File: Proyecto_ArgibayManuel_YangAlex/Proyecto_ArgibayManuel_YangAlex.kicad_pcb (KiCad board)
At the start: 2 copper layers, 56 parts, among them IC1 LM1117, J1 Con_1x3, J2 Con_1x2, J3 Con_1x3, J4 Conn_01x03_Pin, J5 Conn_01x06, J6 Con_ICSP, K1 RT314012, K2 RT314012, Q1 2N2222, Q2 2N2222, SW1 SW_Push, SW2 SW_Push, SW3 SW_Push, SW4 SW_Push, U1 PIC18F258-I_SO, U2 HDC2010YPAR, U3 LT1716IS5TRMPBF, U4 LT1716IS5TRMPBF, U5 TXS0108EPW, U6 DRV8871DDA, U7 DRV8871DDA, U8 MCP2551-I-P, X1 DB9, X2 DB9, Y1 Crystal

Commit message: Conexiones(no acabado)
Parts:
- removed R10: 0, Resistor_SMD:R_0805_2012Metric
- moved J2 174.3 mm to (61.5, 63.7)
- moved J1 170.0 mm to (61.5, 51.5)
- moved J3 165.8 mm to (61.0, 80.0), turned to 180 degrees
- moved D3 106.6 mm to (83.5, 61.5), turned to 90 degrees
- moved J6 102.9 mm to (61.5, 85.2)
- moved R4 96.4 mm to (184.4, 132.8), turned to 180 degrees
- moved C8 95.5 mm to (90.0, 61.5), turned to -90 degrees
- moved IC1 94.8 mm to (107.5, 53.0), turned to -90 degrees
- moved R6 94.6 mm to (184.4, 135.5), turned to 180 degrees
- moved D4 94.4 mm to (104.5, 63.5), turned to -90 degrees
- moved R5 93.3 mm to (184.4, 129.9), turned to 180 degrees
- moved C9 92.1 mm to (97.5, 61.5), turned to -90 degrees
- moved R7 89.2 mm to (184.4, 127.0), turned to 180 degrees
- moved R12 87.4 mm to (118.0, 62.4), turned to 90 degrees
- moved C10 85.8 mm to (110.0, 61.5), turned to -90 degrees
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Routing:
- net VCC: track 0.00 -> 298.6 mm
- net VBat: track 0.00 -> 205.0 mm
- net +3.3V: track 0.00 -> 122.9 mm
- net RC7: track 0.00 -> 73.3 mm
- net RC6: track 0.00 -> 70.2 mm
- net PGC: track 0.00 -> 64.7 mm
- net PGD: track 0.00 -> 64.6 mm
- net Int_Bomba_de_Agua: track 0.00 -> 58.1 mm
- net CANH: track 0.00 -> 51.0 mm
- net Int_Calefactor: track 0.00 -> 47.8 mm
- net Int_limpiaparabrisas: track 0.00 -> 45.7 mm
- net CANL: track 0.00 -> 42.2 mm
- net Net-(U2-VDD): track 0.00 -> 34.3 mm
- net VPP: track 0.00 -> 28.6 mm
- net Net-(D3-K): track 0.00 -> 27.6 mm
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- added copper zone on B.Cu, net (none)

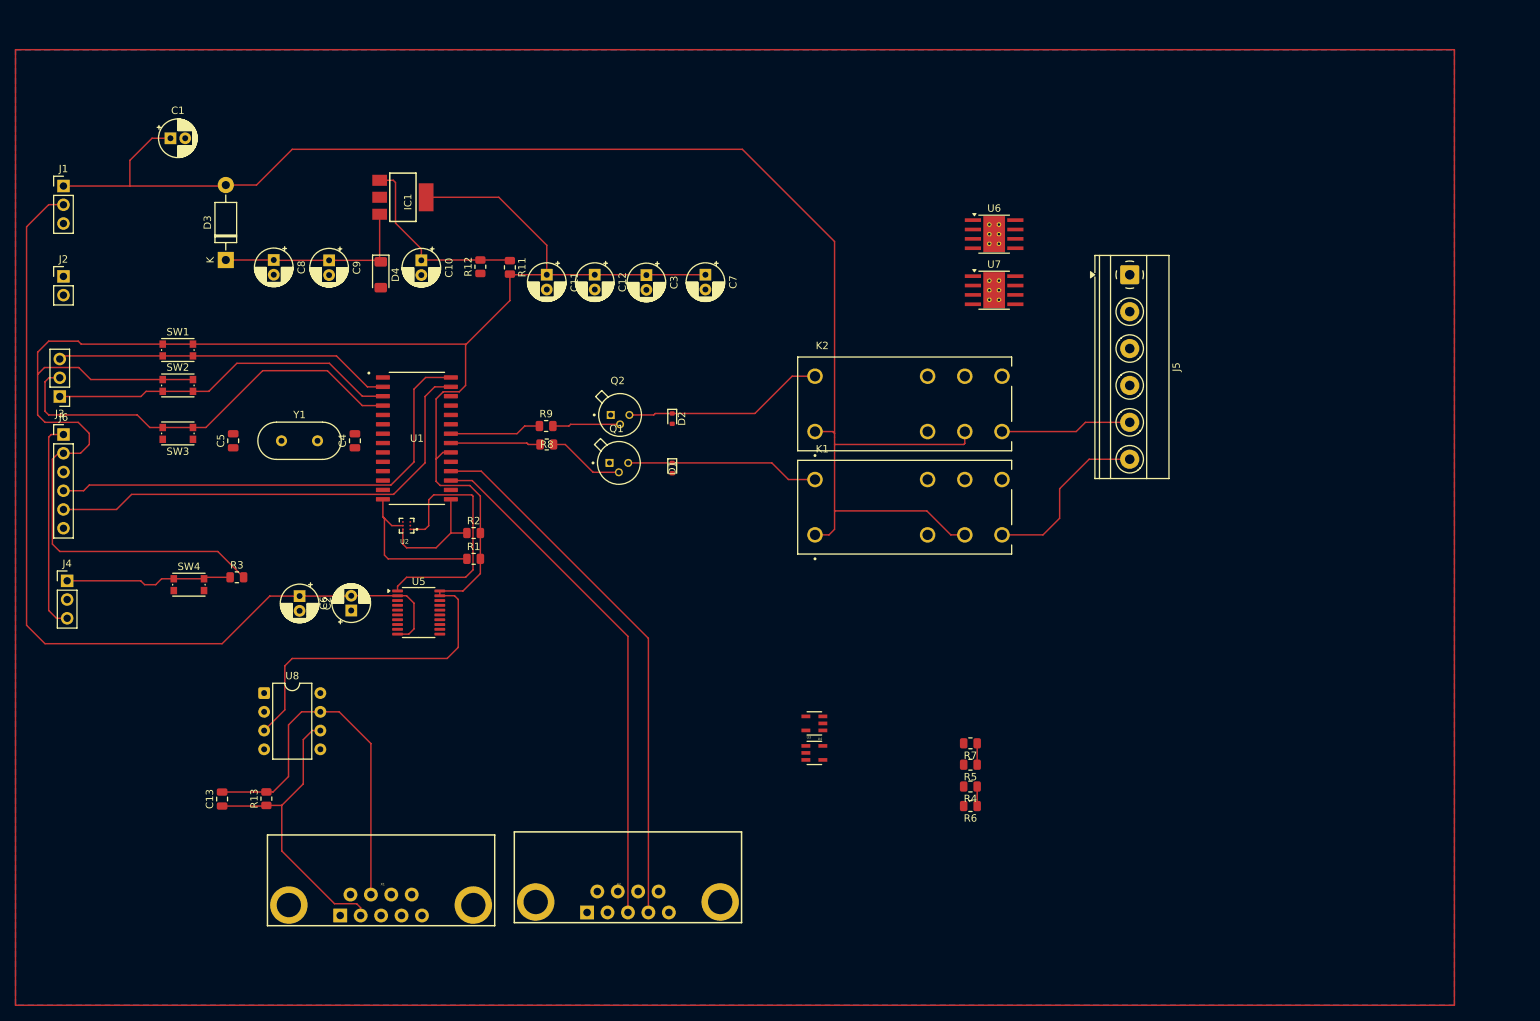
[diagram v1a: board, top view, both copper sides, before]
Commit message: Cambio layout (faltan agregar vías y reorganizar con la capa BOTTOM)
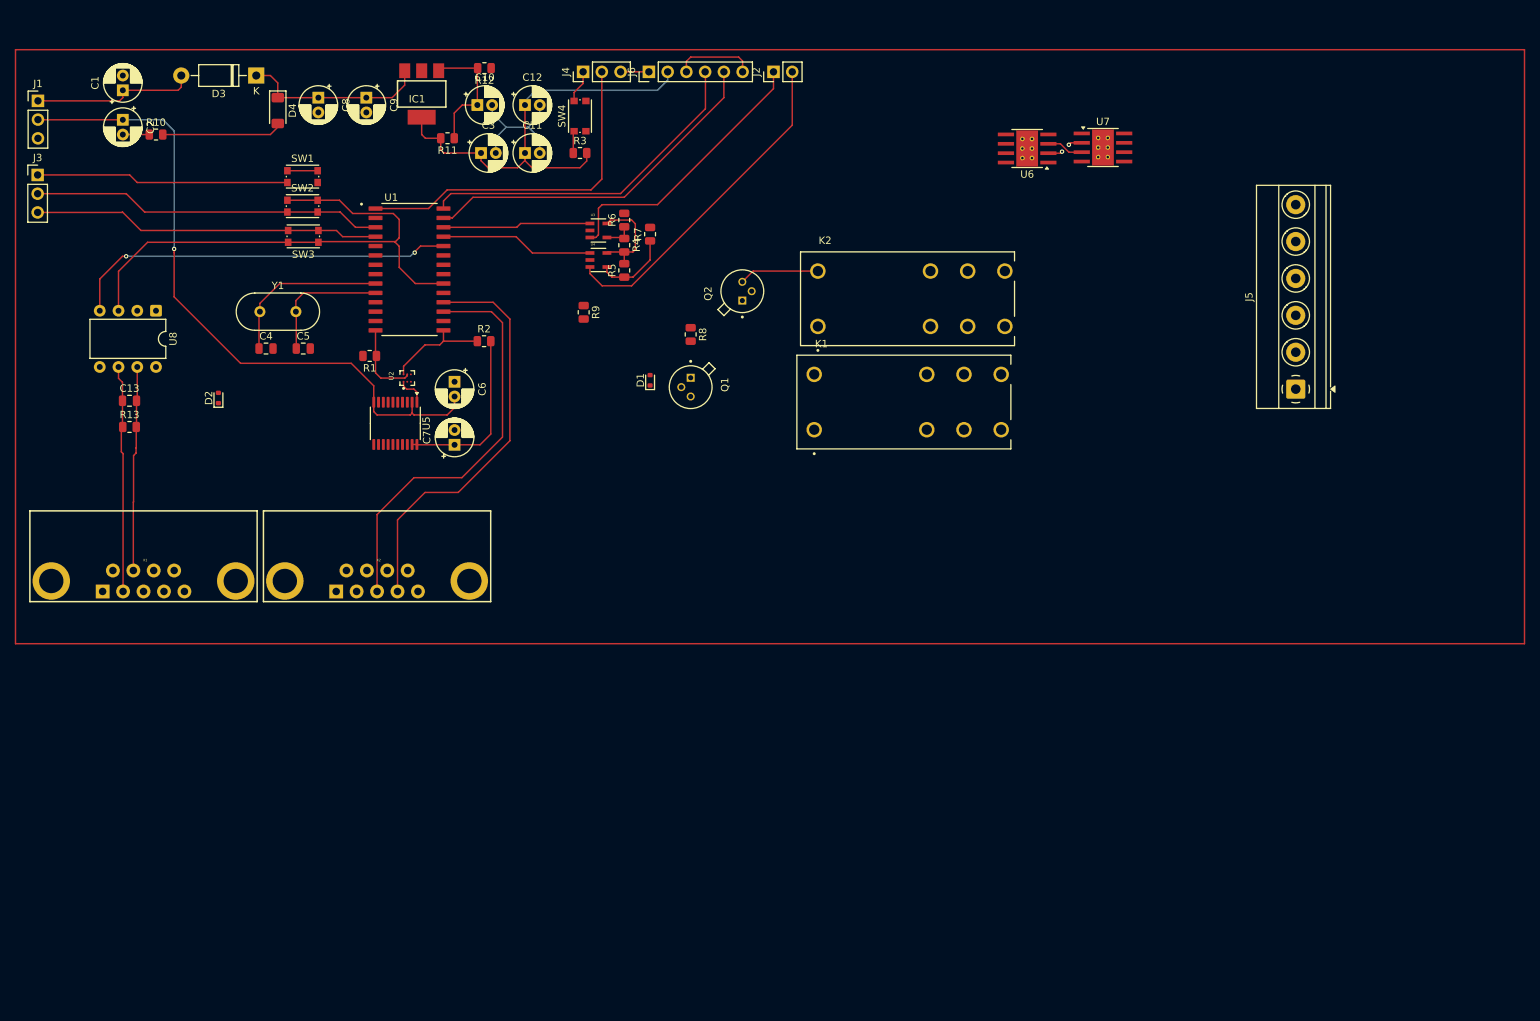
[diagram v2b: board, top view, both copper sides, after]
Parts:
- added R10: 0, Resistor_SMD:R_0805_2012Metric, F.Cu at (74.0, 44.5)
- moved J2 100.1 mm to (157.7, 36.0), turned to 90 degrees
- moved J4 98.2 mm to (131.9, 36.0), turned to 90 degrees
- moved J6 93.3 mm to (140.8, 36.0), turned to 90 degrees
- moved R6 92.2 mm to (137.5, 56.1), turned to 90 degrees
- moved R4 87.1 mm to (137.5, 59.5), turned to -90 degrees
- moved SW4 82.7 mm to (131.5, 42.0), turned to 90 degrees
- moved R5 81.8 mm to (137.5, 62.9), turned to 90 degrees
- moved R7 81.5 mm to (141.0, 58.0), turned to 90 degrees
- moved U3 76.6 mm to (134.0, 57.5)
- moved R3 73.9 mm to (131.5, 47.0)
- moved U4 69.3 mm to (134.0, 61.5), turned to 0 degrees
- moved C2 68.8 mm to (69.5, 42.5)
- moved D2 61.6 mm to (82.5, 80.2), turned to 90 degrees
- moved C13 55.4 mm to (70.5, 80.6), turned to 0 degrees
- moved X2 55.2 mm to (104.0, 105.0)
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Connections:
- J2 pad 1: F_C_In1 -> F_C_In2
- J2 pad 2: F_C_In2 -> F_C_In1
- J3 pad 1: Int_Calefactor -> Int_limpiaparabrisas
- J3 pad 2: Int_Bomba_de_Agua -> Int_Calefactor
- J3 pad 3: Int_limpiaparabrisas -> Int_Bomba_de_Agua
- U6 pad 6: Motor_Izquierdo_1 -> Motor_izquierdo_2
- U6 pad 8: Motor_izquierdo_2 -> Motor_Izquierdo_1
- U7 pad 6: Motor_derecho_1 -> Motor_derecho_2
- U7 pad 8: Motor_derecho_2 -> Motor_derecho_1
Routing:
- net VBat: track 205.0 -> 21.9 mm
- net VCC: track 298.6 -> 176.6 mm
- net RX: track 0.00 -> 52.8 mm, vias 0 -> 2
- net MCLR: track 0.00 -> 46.9 mm
- net F_C_In1: track 0.00 -> 45.2 mm
- net F_C_In2: track 0.00 -> 37.6 mm
- net GND: track 0.00 -> 33.6 mm
- net +3.3V: track 122.9 -> 91.9 mm, vias 0 -> 1
- net Net-(U2-VDD): track 34.3 -> 4.11 mm
- net Net-(D1-K): track 26.2 -> 0.00 mm
- net VPP: track 28.6 -> 3.84 mm
- net Bomba: track 23.9 -> 0.00 mm
- net CANH: track 51.0 -> 27.9 mm
- net TX1: track 0.00 -> 23.0 mm
- net F_C_Out1: track 0.00 -> 20.8 mm
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- removed copper zone on B.Cu, net (none)

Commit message: Termino layout (faltan acomodar etiquetas en la pcb))
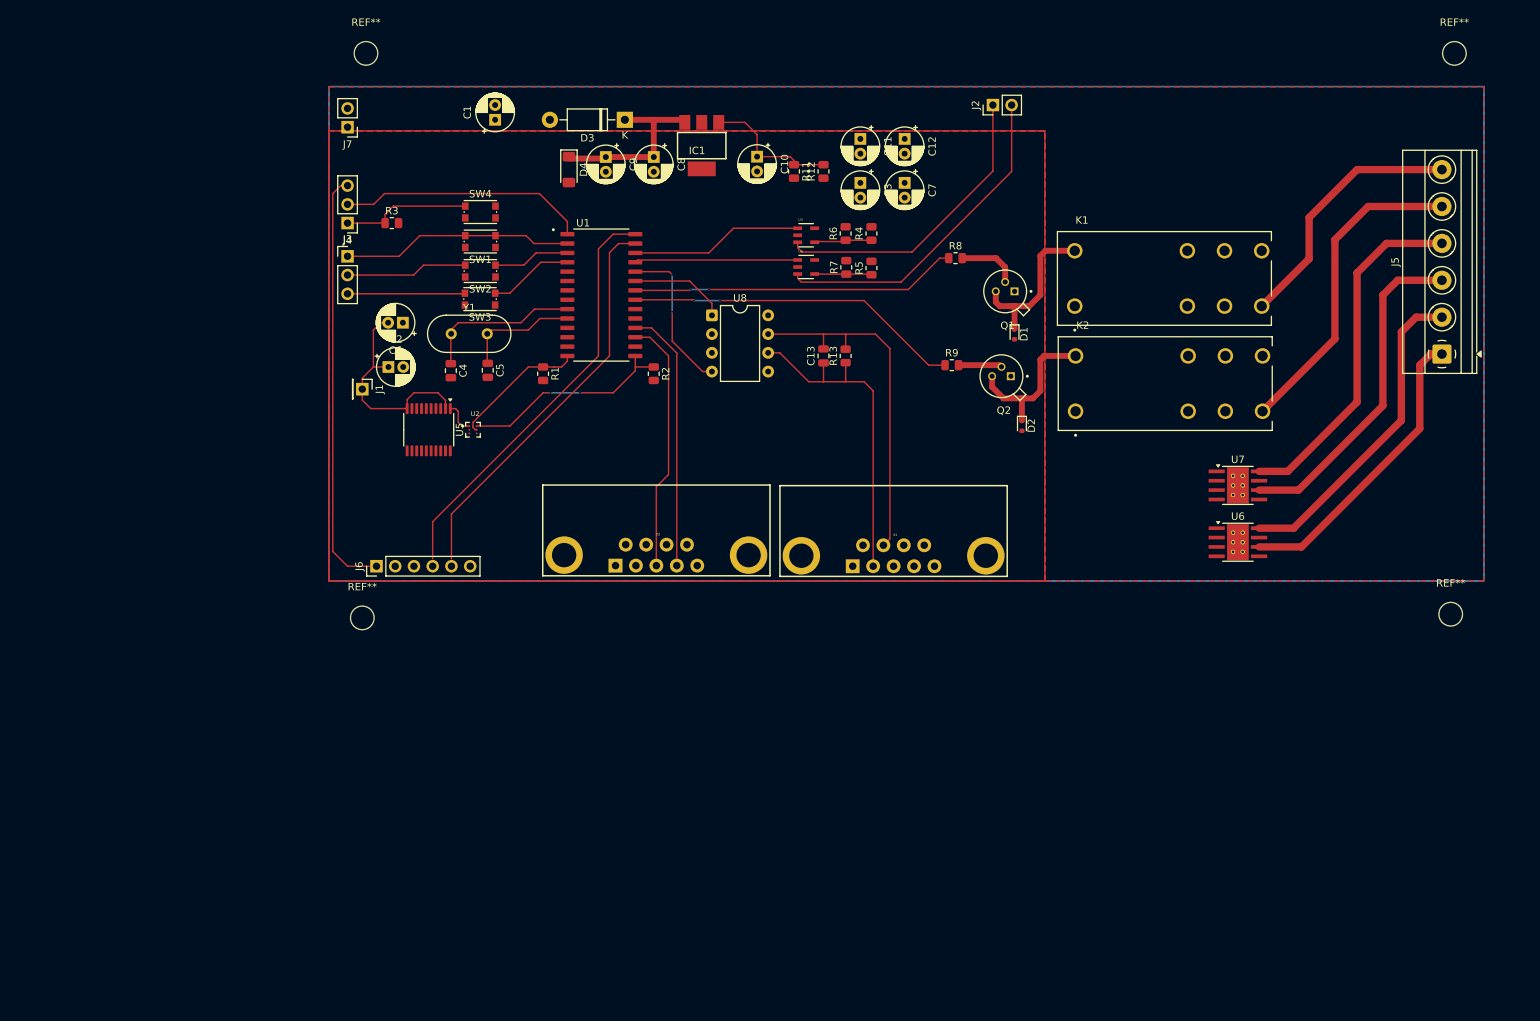
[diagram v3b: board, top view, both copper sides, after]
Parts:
- removed R10: 0, Resistor_SMD:R_0805_2012Metric
- added J7: Conn_01x02, Connector_PinHeader_2.54mm:PinHeader_1x02_P2.54mm_Vertical, F.Cu at (100.0, 43.5)
- added REF**: MountingHole_3.2mm_M3, MountingHole:MountingHole_3.2mm_M3, F.Cu at (102.0, 110.0)
- added REF**: MountingHole_3.2mm_M3, MountingHole:MountingHole_3.2mm_M3, F.Cu at (249.5, 109.5)
- added REF**: MountingHole_3.2mm_M3, MountingHole:MountingHole_3.2mm_M3, F.Cu at (102.5, 33.5)
- added REF**: MountingHole_3.2mm_M3, MountingHole:MountingHole_3.2mm_M3, F.Cu at (250.0, 33.5)
- J1: value Con_1x3 -> Conn_01x01; footprint Connector_PinHeader_2.54mm:PinHeader_1x03_P2.54mm_Vertical -> Connector_PinHeader_2.54mm:PinHeader_1x01_P2.54mm_Vertical
- moved D2 109.0 mm to (191.4, 84.0), turned to -90 degrees
- moved X1 101.7 mm to (174.0, 101.6)
- moved R13 97.5 mm to (167.5, 74.5), turned to 90 degrees
- moved C13 94.2 mm to (164.5, 74.5), turned to 90 degrees
- moved J6 76.5 mm to (103.9, 103.0)
- moved U8 75.3 mm to (149.4, 69.0), turned to 0 degrees
- moved C7 70.6 mm to (175.5, 51.0), turned to -90 degrees
- moved U6 60.5 mm to (220.7, 99.8), turned to 0 degrees
- moved J1 58.8 mm to (102.0, 79.0), turned to -90 degrees
- moved C12 51.7 mm to (175.5, 45.1), turned to -90 degrees
- moved C3 51.6 mm to (169.5, 51.0), turned to -90 degrees
- moved C1 50.6 mm to (120.0, 42.5)
- moved R9 50.4 mm to (181.9, 75.8), turned to 0 degrees
- moved D3 50.3 mm to (137.6, 42.5)
- moved D1 49.8 mm to (190.4, 71.5), turned to -90 degrees
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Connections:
- J1 pad 1: VBat -> +3.3V
- U1 pad 21: C_R_Bombas_agua -> C_R_Calefactor
- U1 pad 22: C_R_Calefactor -> C_R_Bombas_agua
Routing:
- net VCC: track 176.6 -> 0.00 mm
- net +3.3V: track 91.9 -> 29.5 mm, vias 1 -> 0
- net VPP: track 3.84 -> 57.7 mm
- net Motor_derecho_1: track 0.00 -> 47.8 mm
- net C_R_Calefactor: track 0.00 -> 45.6 mm, vias 0 -> 2
- net Motor_derecho_2: track 0.00 -> 45.3 mm
- net C_R_Bombas_agua: track 0.00 -> 44.3 mm, vias 0 -> 2
- net Calefactor: track 0.00 -> 43.7 mm
- net Motor_Izquierdo_1: track 0.00 -> 43.6 mm
- net Motor_izquierdo_2: track 0.00 -> 40.6 mm
- net Bomba: track 0.00 -> 35.4 mm
- net GND: track 33.6 -> 0.00 mm
- net RX: track 52.8 -> 21.3 mm
- net VBat: track 21.9 -> 0.00 mm
- net Net-(D1-K): track 0.00 -> 21.7 mm
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- added copper zone on B.Cu, net GND
- added copper zone on F.Cu, net VBat
- added copper zone on F.Cu, net VCC

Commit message: Arreglo nodos no conectados
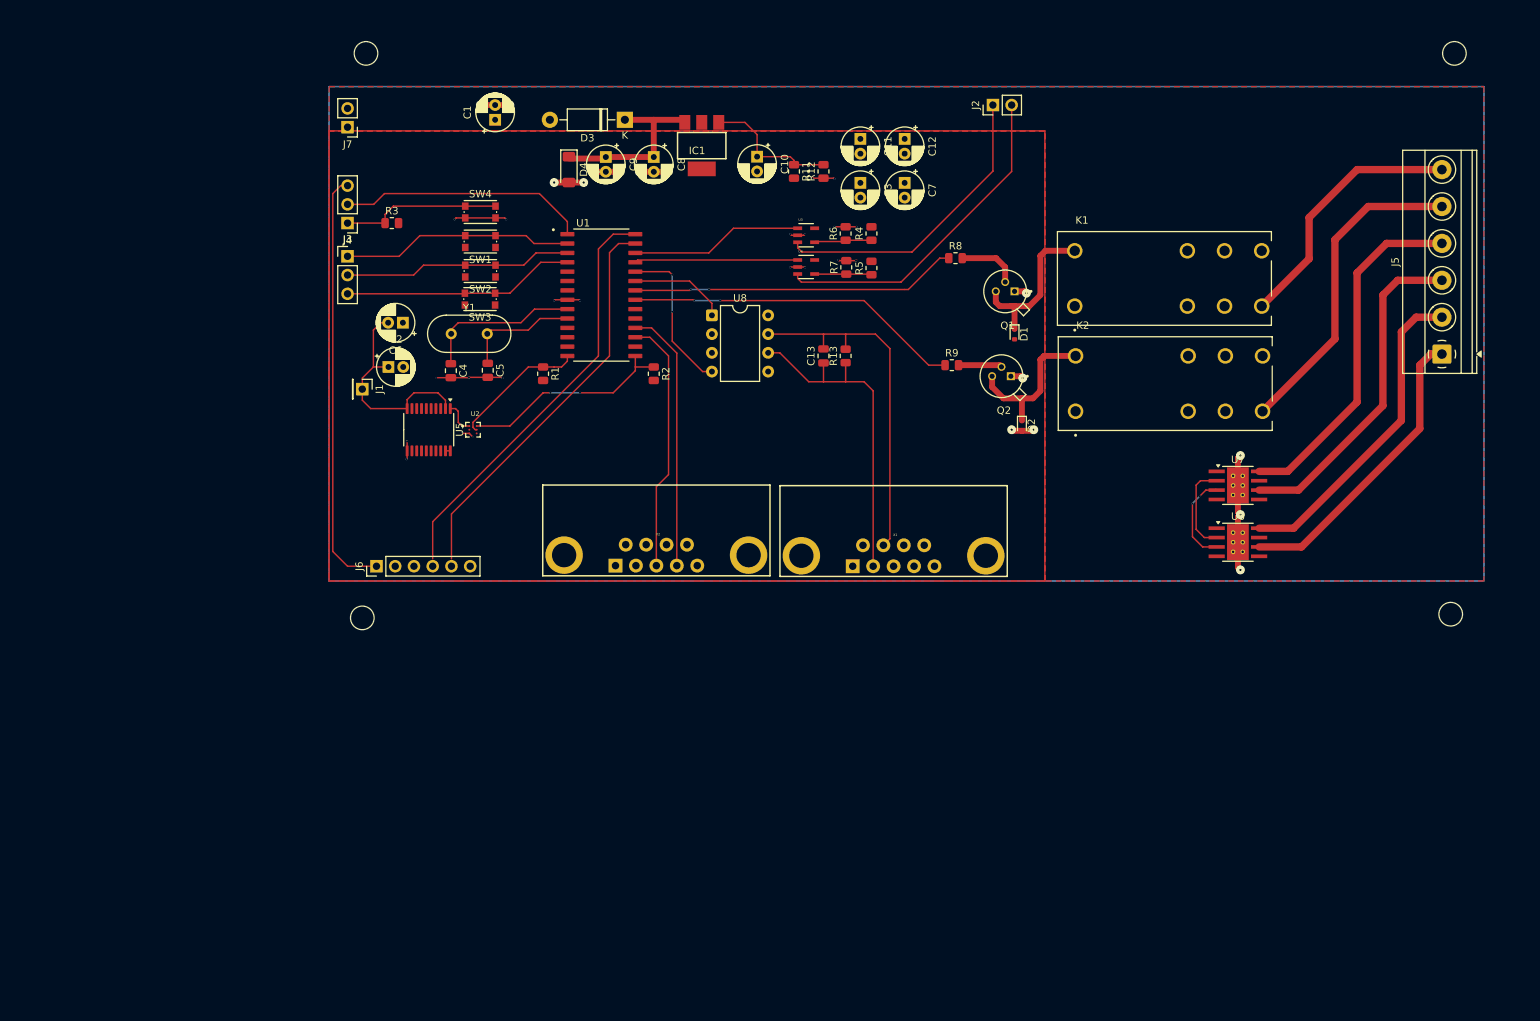
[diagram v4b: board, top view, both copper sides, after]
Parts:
- renumbered REF** to Ref
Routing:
- net GNDPWR: track 0.00 -> 38.2 mm, vias 0 -> 15
- net GND: track 0.00 -> 37.0 mm, vias 0 -> 21
- net PH_M_in1: track 0.19 -> 12.6 mm, vias 0 -> 2
- net PH_M_in2: track 0.00 -> 12.3 mm
- net Int_Calefactor: track 26.9 -> 31.0 mm
- net Net-(J4-Pin_1): track 17.6 -> 21.7 mm
- net Int_Bomba_de_Agua: track 27.5 -> 31.6 mm
- net VCC: track 0.00 -> 0.65 mm
